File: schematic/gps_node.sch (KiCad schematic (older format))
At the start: 78 parts, among them IC1 MMA8452Q, IC2 MCP73831/2, J1 USB_OTG, J10 Mounting Hole, J11 TEST Vbatt, J12 Test 3.3v, J13 Test Gnd, J14 UART RF, J15 I2C GPS, J16 UART GPS, J17 GPIO_0, J18 GPIO_1, J2 AVR ICSP, J3 LIPO_BAT, J4 SOLAR, J5 FW_UPDATE, J6 SMA, J7 Mounting Hole, J8 Mounting Hole, J9 Mounting Hole, SW1 SW_SP3T, SW2 RESET, U1 TLV71333PDBV, U2 ublox-cam-m8q-0, U3 ATMEGA32U4-AU, U4 RN2483, Y1 16MHz

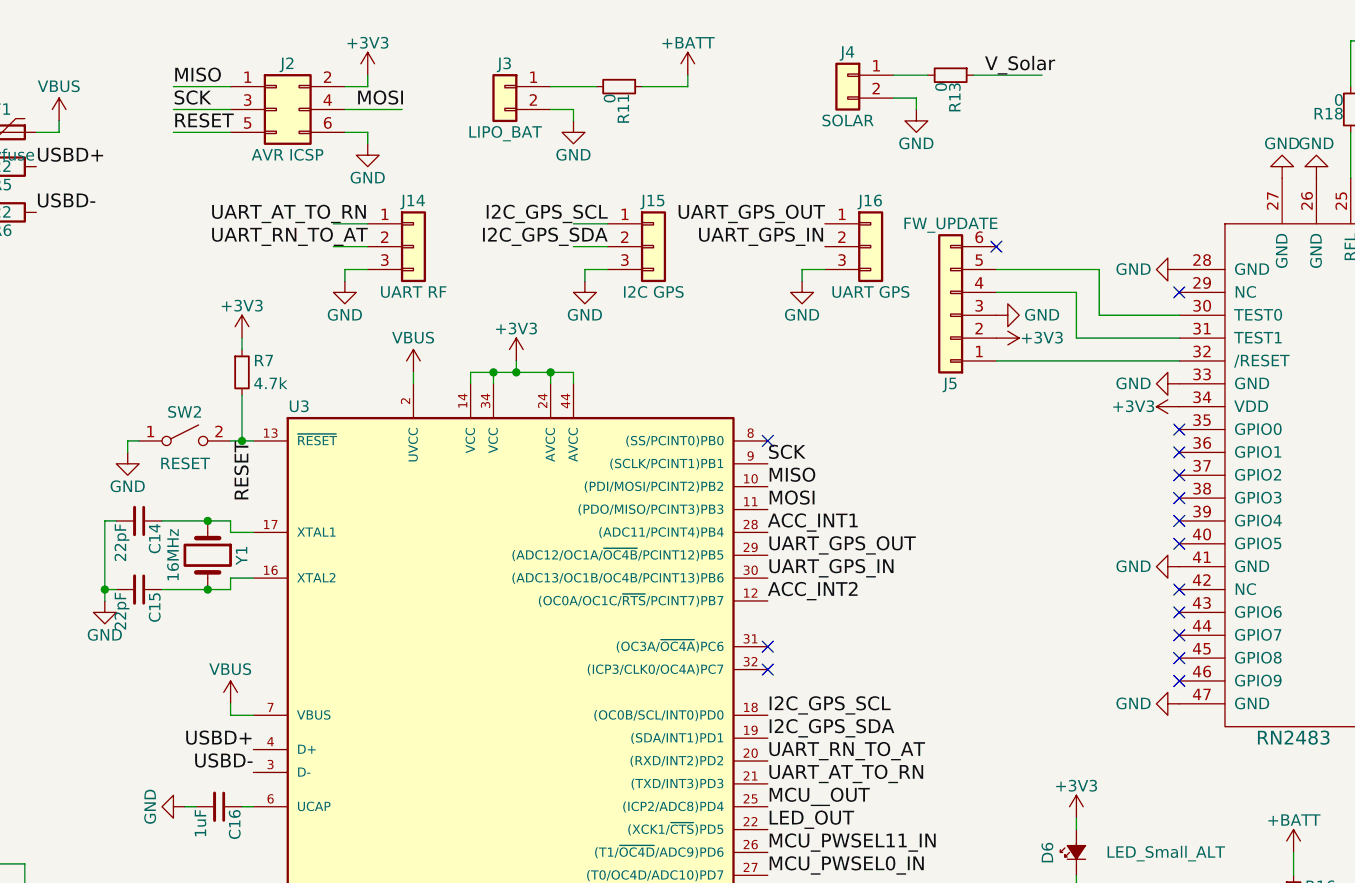
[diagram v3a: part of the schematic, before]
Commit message: Issue #2: Adds RN2483 reset pin
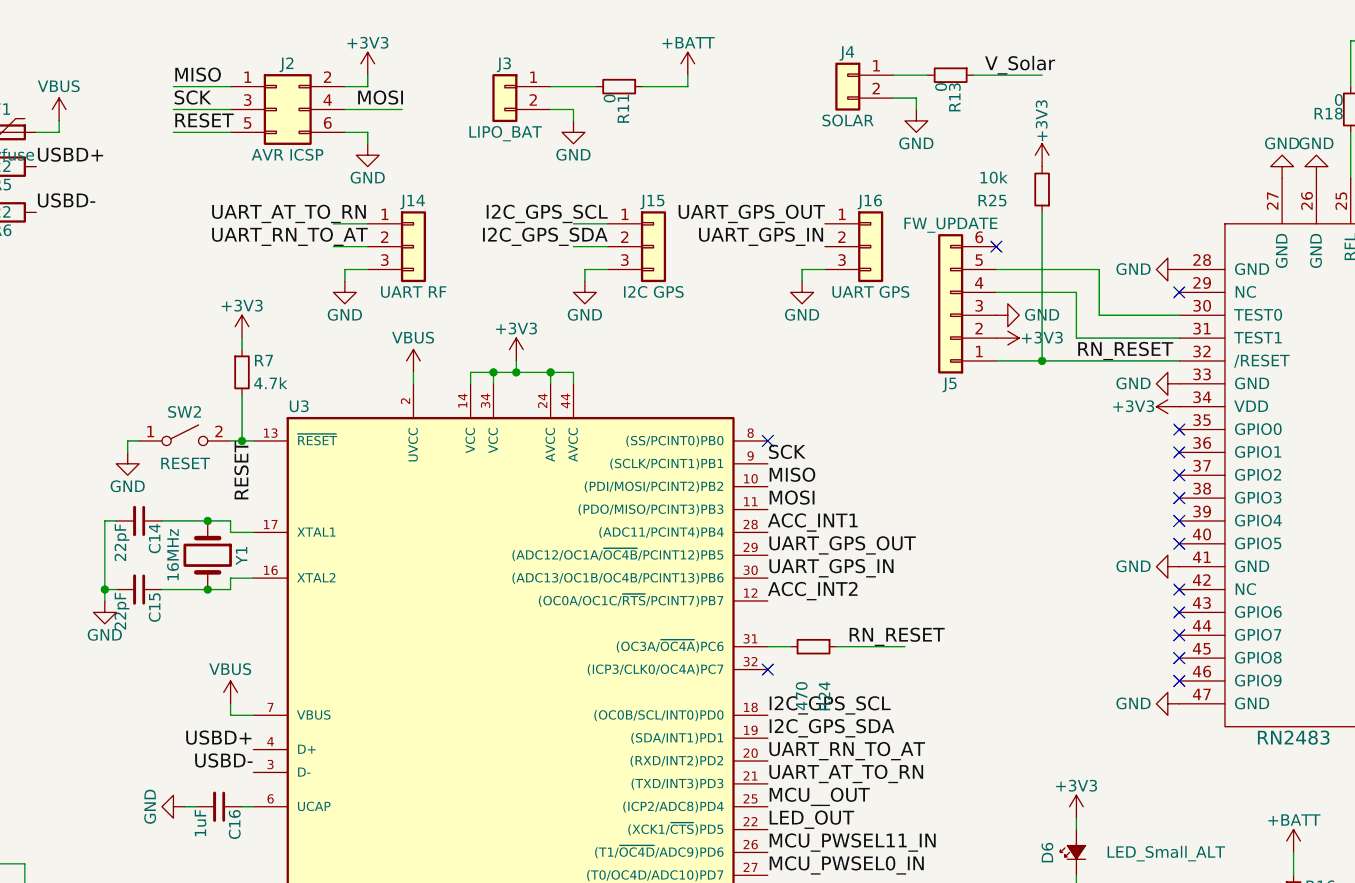
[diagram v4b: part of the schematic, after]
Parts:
- added R24: 470, Resistors_SMD:R_0805, symbol R_Small
- added R25: 10k, Resistors_SMD:R_0805, symbol R_Small
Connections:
- net labels added: RN_RESET
- wire segments 231 -> 234
- no-connect marks 52 -> 51

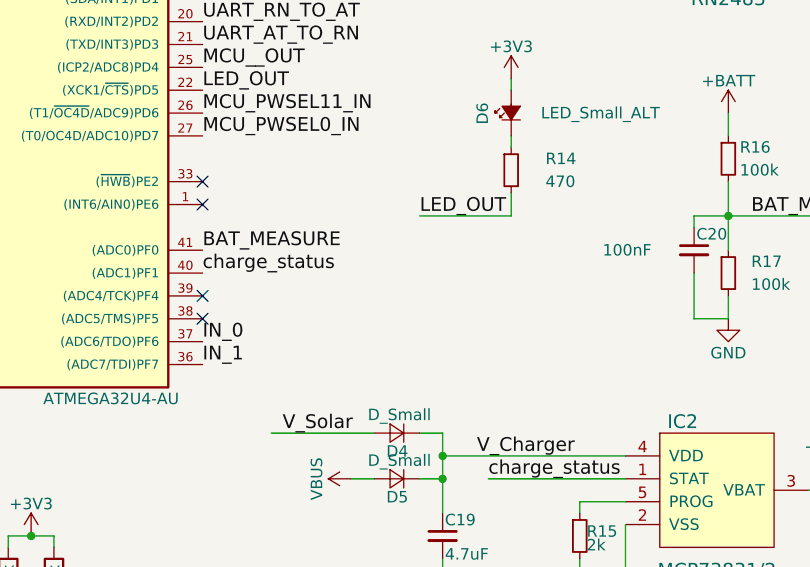
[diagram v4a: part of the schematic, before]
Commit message: Adds RGB led, updates schematic
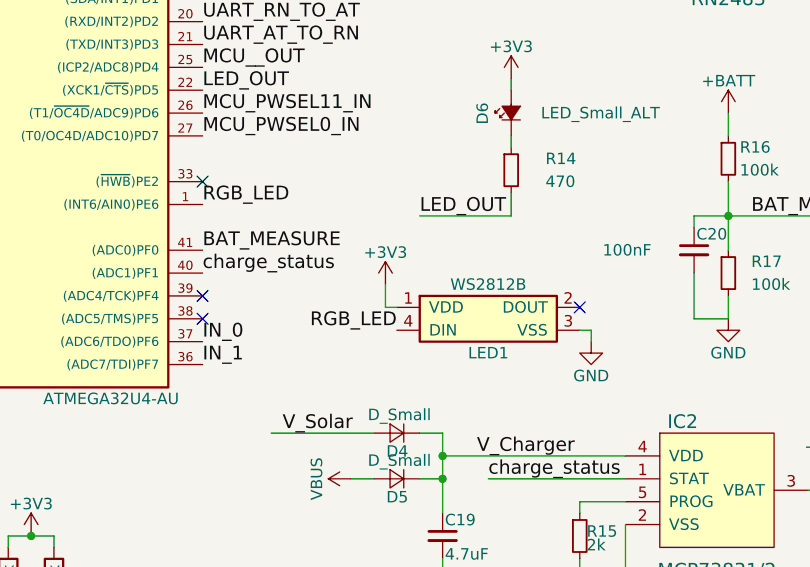
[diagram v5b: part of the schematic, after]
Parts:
- added LED1: WS2812B, LEDs:LED_WS2812B-PLCC4, symbol WS2812B
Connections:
- net labels added: RGB_LED
- wire segments 234 -> 238
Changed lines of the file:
@@
 $EndComp
 NoConn ~ 6800 5050
-NoConn ~ 6800 4550
 NoConn ~ 6800 4450
 NoConn ~ 6800 3350
@@
 	1    0    0    -1
 $EndComp
+$Comp
+L WS2812B LED1
+U 1 1 5AB809E4
+P 8050 5000
+F 0 "LED1" H 8050 4800 50  0000 C CNN
+F 1 "WS2812B" H 8050 5100 50  0000 C CNN
+F 2 "LEDs:LED_WS2812B-PLCC4" H 8050 4700 50  0001 C CNN
+F 3 "" H 8050 4950 50  0001 C CNN
+	1    8050 5000
+	1    0    0    -1
+$EndComp
+Text Label 6800 4550 0    60   ~ 0
+RGB_LED
+Text Label 7650 5100 2    60   ~ 0
+RGB_LED
+$Comp
+L +3V3 #PWR074
+U 1 1 5AB82068
+P 7600 4900
+F 0 "#PWR074" H 7600 4750 50  0001 C CNN
+F 1 "+3V3" H 7600 5040 50  0000 C CNN
+F 2 "" H 7600 4900 50  0001 C CNN
+F 3 "" H 7600 4900 50  0001 C CNN
+	1    7600 4900
+	1    0    0    -1
+$EndComp
+Wire Wire Line
+	7650 5000 7600 5000
+Wire Wire Line
+	7600 5000 7600 4900
+$Comp
+L GND #PWR075
+U 1 1 5AB83D22
+P 8500 5150
+F 0 "#PWR075" H 8500 4900 50  0001 C CNN
+F 1 "GND" H 8500 5000 50  0000 C CNN
+F 2 "" H 8500 5150 50  0001 C CNN
+F 3 "" H 8500 5150 50  0001 C CNN
+	1    8500 5150
+	1    0    0    -1
+$EndComp
+Wire Wire Line
+	8450 5100 8500 5100
+Wire Wire Line
+	8500 5100 8500 5150
+NoConn ~ 8450 5000
 $EndSCHEMATC

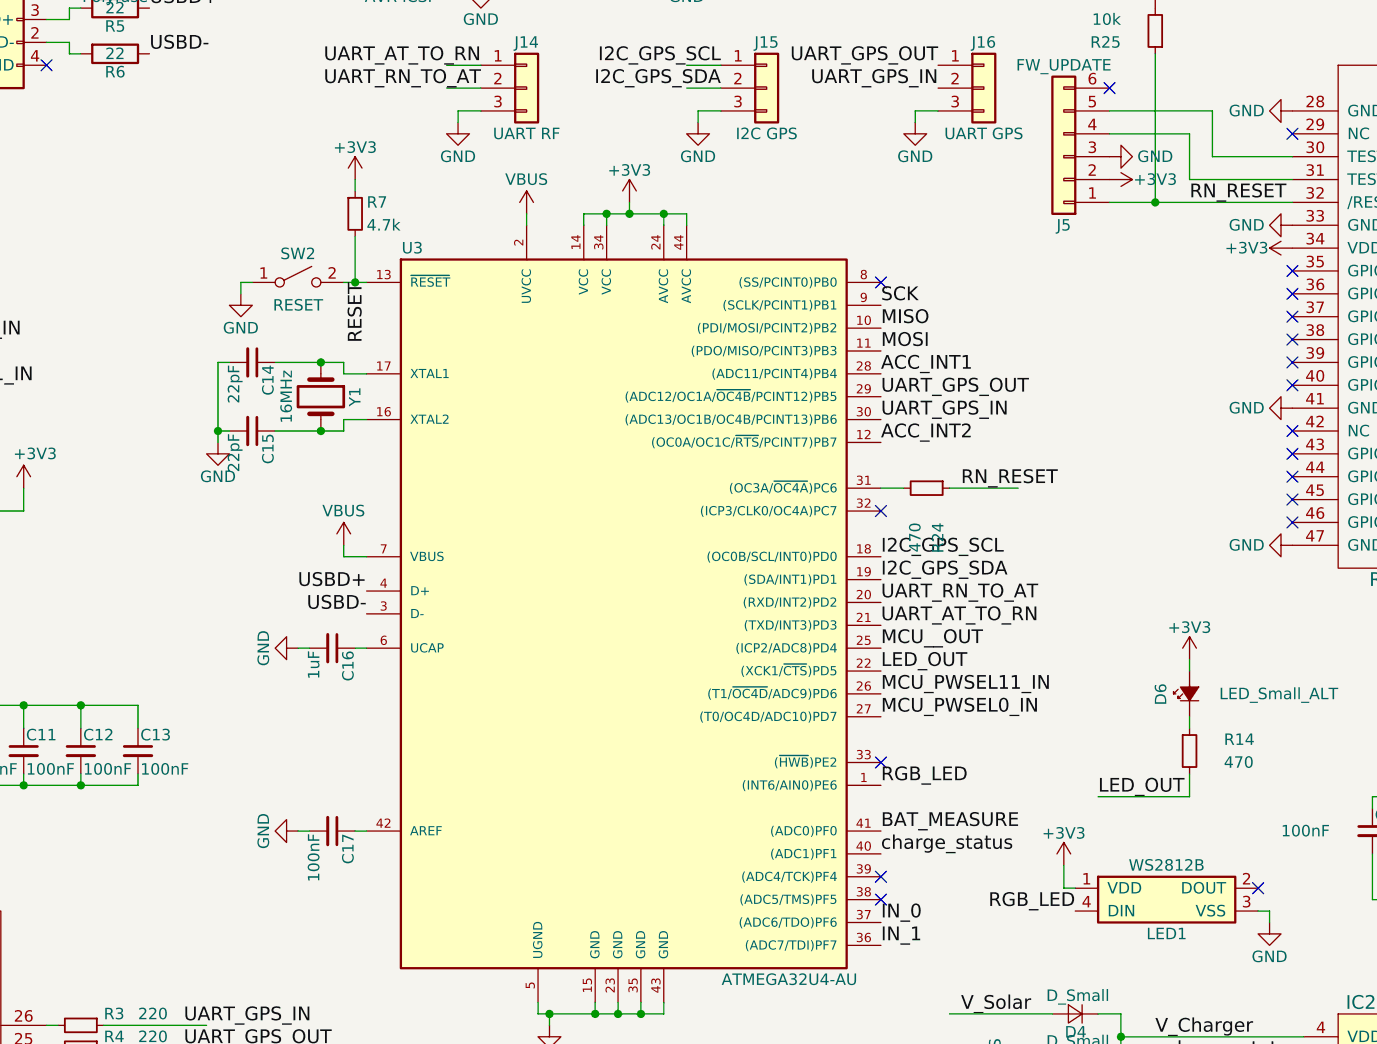
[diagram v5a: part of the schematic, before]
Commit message: Added more group pour aroudd gps, additional buttons
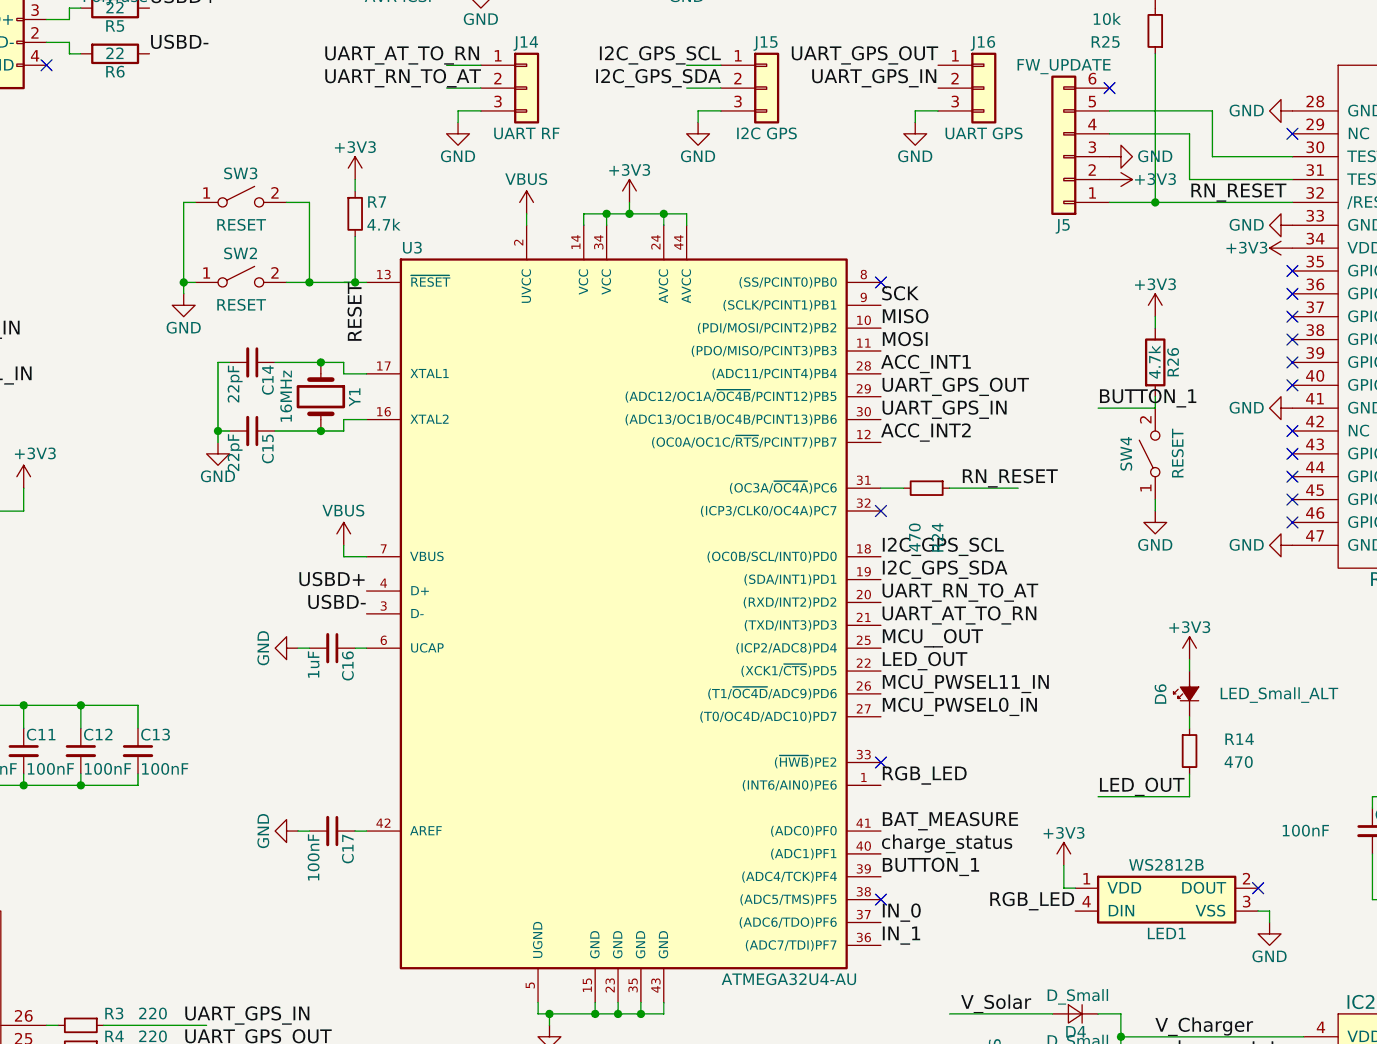
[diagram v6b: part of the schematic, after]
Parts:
- added R26: 4.7k, Resistors_SMD:R_0805, symbol R
- added SW3, SW4: RESET, Buttons_Switches_SMD:SW_SPST_PTS645, symbol SW_SPST
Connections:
- net labels added: BUTTON_1
- wire segments 238 -> 246
- no-connect marks 51 -> 50
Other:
- moved on the sheet: SW2
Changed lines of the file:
@@
 L SW_SPST SW2
 U 1 1 5A2CDA55
-P 4250 2350
-F 0 "SW2" H 4250 2475 50  0000 C CNN
-F 1 "RESET" H 4250 2250 50  0000 C CNN
-F 2 "Buttons_Switches_SMD:SW_SPST_PTS645" H 4250 2350 50  0001 C CNN
-F 3 "" H 4250 2350 50  0001 C CNN
-	1    4250 2350
+P 4000 2350
+F 0 "SW2" H 4000 2475 50  0000 C CNN
+F 1 "RESET" H 4000 2250 50  0000 C CNN
+F 2 "Buttons_Switches_SMD:SW_SPST_PTS645" H 4000 2350 50  0001 C CNN
+F 3 "" H 4000 2350 50  0001 C CNN
+	1    4000 2350
 	1    0    0    -1
 $EndComp
@@
 L GND #PWR036
 U 1 1 5A2CDBA5
-P 4000 2400
-F 0 "#PWR036" H 4000 2150 50  0001 C CNN
-F 1 "GND" H 4000 2250 50  0000 C CNN
-F 2 "" H 4000 2400 50  0001 C CNN
-F 3 "" H 4000 2400 50  0001 C CNN
-	1    4000 2400
+P 3750 2400
+F 0 "#PWR036" H 3750 2150 50  0001 C CNN
+F 1 "GND" H 3750 2250 50  0000 C CNN
+F 2 "" H 3750 2400 50  0001 C CNN
+F 3 "" H 3750 2400 50  0001 C CNN
+	1    3750 2400
 	1    0    0    -1
 $EndComp
@@
 	0    1    1    0
 $EndComp
-NoConn ~ 6800 4950
 Text Label 7150 3250 0    60   ~ 0
 RN_RESET
@@
 	4500 1950 4500 1900
 Wire Wire Line
-	4500 2150 4500 2350
+	4500 2350 4500 2150
 Wire Wire Line
 	4450 2350 4550 2350
@@
 	8150 1700 7800 1700
 Wire Wire Line
-	4000 2400 4000 2350
-Wire Wire Line
-	4000 2350 4050 2350
+	3750 2000 3750 2400
+Wire Wire Line
+	3750 2350 3800 2350
 Connection ~ 4500 2350
 Wire Wire Line
@@
 	8500 5100 8500 5150
 NoConn ~ 8450 5000
+Connection ~ 3750 2350
+Wire Wire Line
+	4300 2000 4300 2350
+Wire Wire Line
+	4200 2350 4500 2350
+Connection ~ 4300 2350
+$Comp
+L SW_SPST SW3
+U 1 1 5ABA55AE
+P 4000 2000
+F 0 "SW3" H 4000 2125 50  0000 C CNN
+F 1 "RESET" H 4000 1900 50  0000 C CNN
+F 2 "Buttons_Switches_SMD:SW_SPST_PTS645" H 4000 2000 50  0001 C CNN
+F 3 "" H 4000 2000 50  0001 C CNN
+	1    4000 2000
+	1    0    0    -1
+$EndComp
+Wire Wire Line
+	4300 2000 4200 2000
+Wire Wire Line
+	3800 2000 3750 2000
+$Comp
+L SW_SPST SW4
+U 1 1 5ABA6502
+P 8000 3100
+F 0 "SW4" H 8000 3225 50  0000 C CNN
+F 1 "RESET" H 8000 3000 50  0000 C CNN
+F 2 "Buttons_Switches_SMD:SW_SPST_PTS645" H 8000 3100 50  0001 C CNN
+F 3 "" H 8000 3100 50  0001 C CNN
+	1    8000 3100
+	0    -1   -1   0
+$EndComp
+$Comp
+L R R26
+U 1 1 5ABA9E78
+P 8000 2700
+F 0 "R26" V 8080 2700 50  0000 C CNN
+F 1 "4.7k" V 8000 2700 50  0000 C CNN
+F 2 "Resistors_SMD:R_0805" V 7930 2700 50  0001 C CNN
+F 3 "" H 8000 2700 50  0001 C CNN
+	1    8000 2700
+	1    0    0    -1
+$EndComp
+$Comp
+L GND #PWR076
+U 1 1 5ABAC75E
+P 8000 3350
+F 0 "#PWR076" H 8000 3100 50  0001 C CNN
+F 1 "GND" H 8000 3200 50  0000 C CNN
+F 2 "" H 8000 3350 50  0001 C CNN
+F 3 "" H 8000 3350 50  0001 C CNN
+	1    8000 3350
+	1    0    0    -1
+$EndComp
+$Comp
+L +3V3 #PWR077
+U 1 1 5ABAFA35
+P 8000 2500
+F 0 "#PWR077" H 8000 2350 50  0001 C CNN
+F 1 "+3V3" H 8000 2640 50  0000 C CNN
+F 2 "" H 8000 2500 50  0001 C CNN
+F 3 "" H 8000 2500 50  0001 C CNN
+	1    8000 2500
+	1    0    0    -1
+$EndComp
+Wire Wire Line
+	8000 2500 8000 2550
+Wire Wire Line
+	8000 2900 8000 2850
+Wire Wire Line
+	8000 3300 8000 3350
+Wire Wire Line
+	8000 2900 7750 2900
+Text Label 7750 2900 0    60   ~ 0
+BUTTON_1
+Text Label 6800 4950 0    60   ~ 0
+BUTTON_1
 $EndSCHEMATC
